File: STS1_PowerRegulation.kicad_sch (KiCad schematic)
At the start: 7 parts, among them U3 MCP1725-3302E_MC

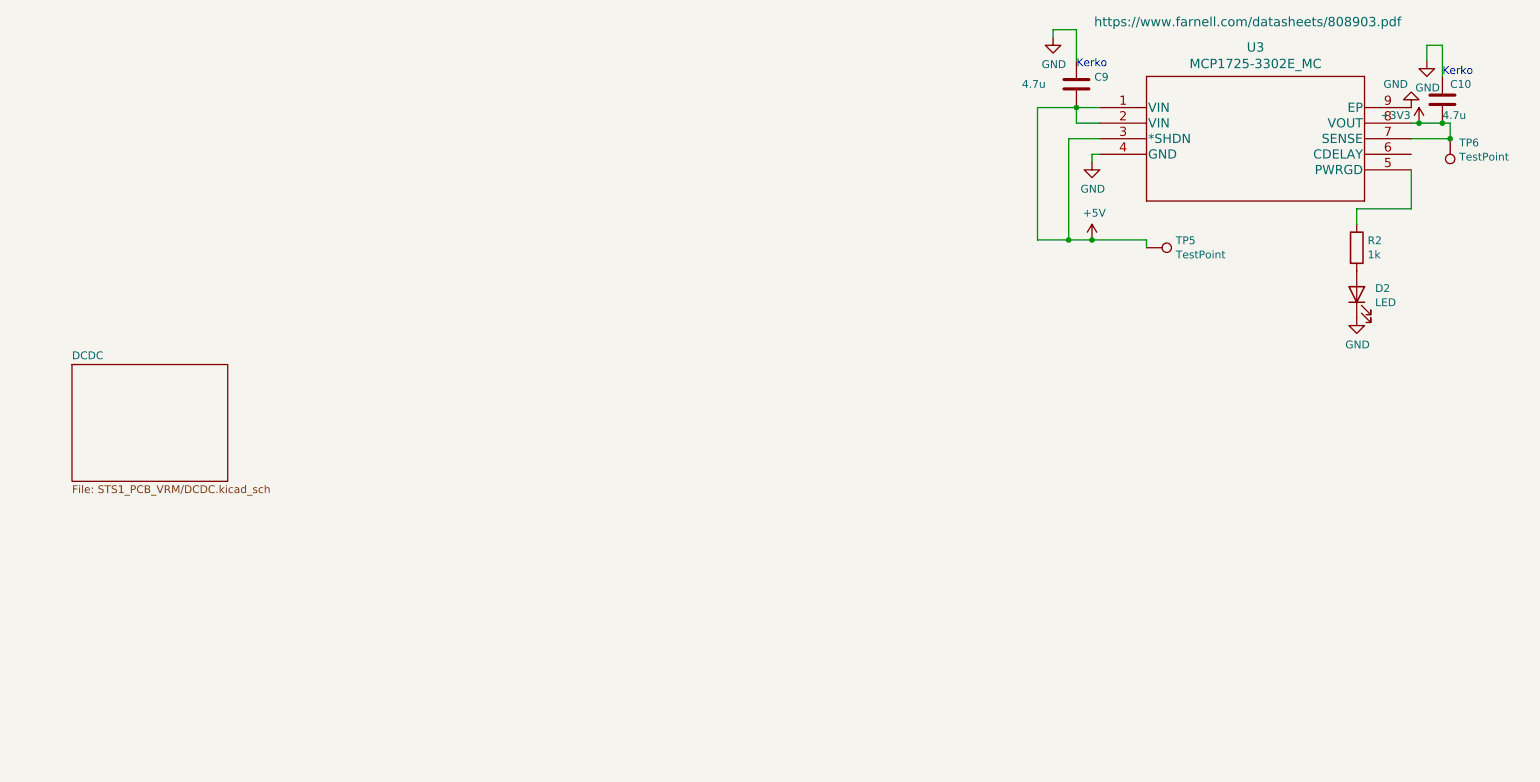
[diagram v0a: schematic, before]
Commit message: more work done
All parts besides RF added
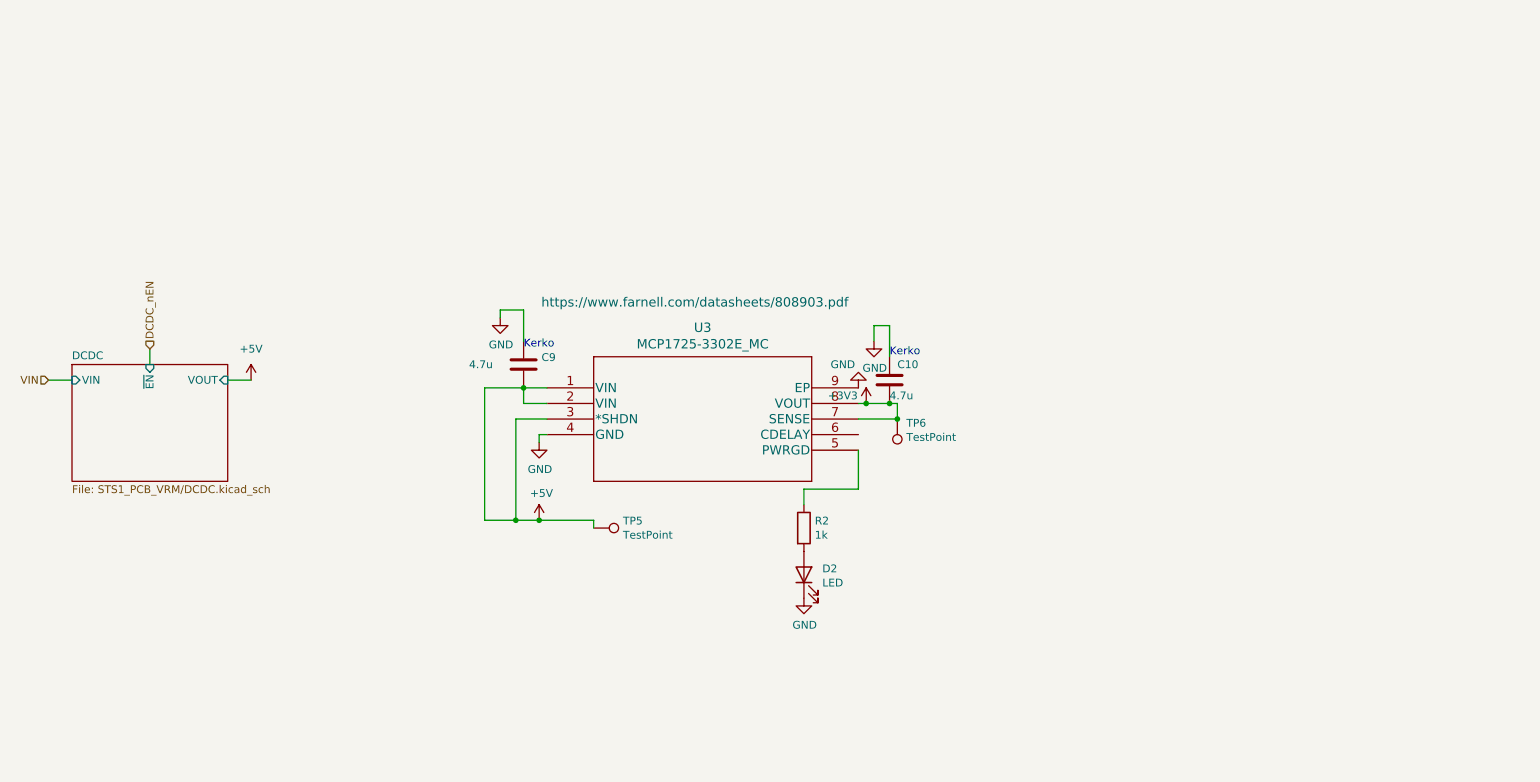
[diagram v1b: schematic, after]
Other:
- sheet DCDC ports: added VIN, VOUT, ~{EN}; removed none
- moved on the sheet: C10, C9, D2, R2, TP5, TP6, U3

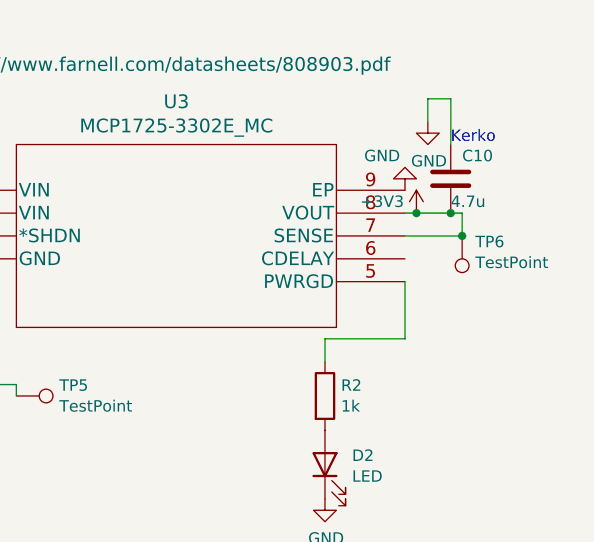
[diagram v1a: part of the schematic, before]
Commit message: add RF part
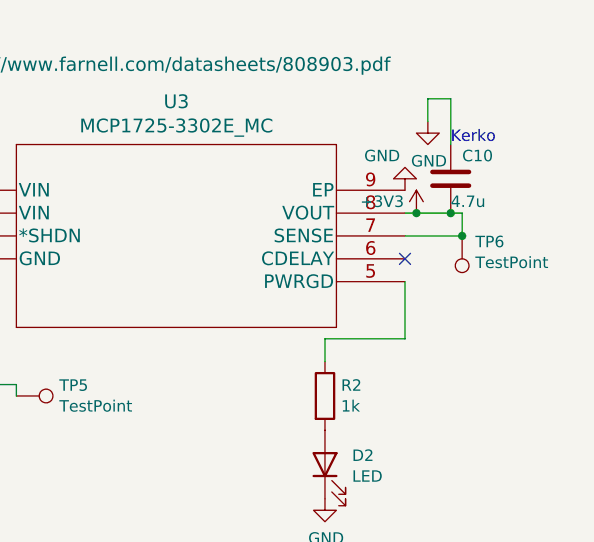
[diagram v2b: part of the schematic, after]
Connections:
- no-connect marks 0 -> 1
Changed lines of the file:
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@@
   (junction (at 130.81 102.87) (diameter 0) (color 0 0 0 0)
   )
+  (no_connect (at 186.69 88.9))
   (wire (pts (xy 83.82 80.01) (xy 87.63 80.01))
     (stroke (width 0) (type default) (color 0 0 0 0))

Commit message: V2.5
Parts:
- added D5, D6: LED, LED_SMD:LED_0805_2012Metric, symbol Device:LED
- added R32, R33: 220R, Resistor_SMD:R_0805_2012Metric, symbol Device:R
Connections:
- net +3V3: now also R33.1
- net +5V: now also R32.1
- net GND: now also D5.1 (K), D6.1 (K)
- new net: D6.2 (A), R33.2
- new net: D5.2 (A), R32.2
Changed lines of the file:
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@@
     (pin "1")
+  )
+  (symbol (lib_id "Device:R") (at 71.12 126.365 0) (unit 1)
+    (in_bom yes) (on_board yes)
+    (property "Reference" "R33" (id 0) (at 72.898 125.1966 0)
+      (effects (font (size 1.27 1.27)) (justify left))
+    )
+    (property "Value" "220R" (id 1) (at 72.898 127.508 0)
+      (effects (font (size 1.27 1.27)) (justify left))
+    )
+    (property "Footprint" "Resistor_SMD:R_0805_2012Metric" (id 2) (at 69.342 126.365 90)
+      (effects (font (size 1.27 1.27)) hide)
+    )
+    (property "Datasheet" "~" (id 3) (at 71.12 126.365 0)
+      (effects (font (size 1.27 1.27)) hide)
+    )
+    (pin "1")
+    (pin "2")
+  )
+  (symbol (lib_id "power:+3V3") (at 71.12 122.555 0) (unit 1)
+    (in_bom yes) (on_board yes) (fields_autoplaced)
+    (property "Reference" "#PWR037" (id 0) (at 71.12 126.365 0)
+      (effects (font (size 1.27 1.27)) hide)
+    )
+    (property "Value" "+3V3" (id 1) (at 71.12 116.84 0))
+    (property "Footprint" "" (id 2) (at 71.12 122.555 0)
+      (effects (font (size 1.27 1.27)) hide)
+    )
+    (property "Datasheet" "" (id 3) (at 71.12 122.555 0)
+      (effects (font (size 1.27 1.27)) hide)
+    )
+    (pin "1")
+  )
+  (symbol (lib_id "Device:LED") (at 57.15 133.985 90) (unit 1)
+    (in_bom yes) (on_board yes)
+    (property "Reference" "D5" (id 0) (at 60.1472 132.9944 90)
+      (effects (font (size 1.27 1.27)) (justify right))
+    )
+    (property "Value" "LED" (id 1) (at 60.1472 135.3058 90)
+      (effects (font (size 1.27 1.27)) (justify right))
+    )
+    (property "Footprint" "LED_SMD:LED_0805_2012Metric" (id 2) (at 57.15 133.985 0)
+      (effects (font (size 1.27 1.27)) hide)
+    )
+    (property "Datasheet" "~" (id 3) (at 57.15 133.985 0)
+      (effects (font (size 1.27 1.27)) hide)
+    )
+    (pin "1")
+    (pin "2")
   )
   (symbol (lib_id "power:+5V") (at 87.63 80.01 0) (unit 1)
@@
     (pin "1")
   )
+  (symbol (lib_id "power:GND") (at 71.12 137.795 0) (unit 1)
+    (in_bom yes) (on_board yes)
+    (property "Reference" "#PWR038" (id 0) (at 71.12 144.145 0)
+      (effects (font (size 1.27 1.27)) hide)
+    )
+    (property "Value" "GND" (id 1) (at 71.247 142.1892 0))
+    (property "Footprint" "" (id 2) (at 71.12 137.795 0)
+      (effects (font (size 1.27 1.27)) hide)
+    )
+    (property "Datasheet" "" (id 3) (at 71.12 137.795 0)
+      (effects (font (size 1.27 1.27)) hide)
+    )
+    (pin "1")
+  )
+  (symbol (lib_id "power:+5V") (at 57.15 122.555 0) (unit 1)
+    (in_bom yes) (on_board yes) (fields_autoplaced)
+    (property "Reference" "#PWR028" (id 0) (at 57.15 126.365 0)
+      (effects (font (size 1.27 1.27)) hide)
+    )
+    (property "Value" "+5V" (id 1) (at 57.15 116.84 0))
+    (property "Footprint" "" (id 2) (at 57.15 122.555 0)
+      (effects (font (size 1.27 1.27)) hide)
+    )
+    (property "Datasheet" "" (id 3) (at 57.15 122.555 0)
+      (effects (font (size 1.27 1.27)) hide)
+    )
+    (pin "1")
+  )
+  (symbol (lib_id "power:GND") (at 57.15 137.795 0) (unit 1)
+    (in_bom yes) (on_board yes)
+    (property "Reference" "#PWR029" (id 0) (at 57.15 144.145 0)
+      (effects (font (size 1.27 1.27)) hide)
+    )
+    (property "Value" "GND" (id 1) (at 57.277 142.1892 0))
+    (property "Footprint" "" (id 2) (at 57.15 137.795 0)
+      (effects (font (size 1.27 1.27)) hide)
+    )
+    (property "Datasheet" "" (id 3) (at 57.15 137.795 0)
+      (effects (font (size 1.27 1.27)) hide)
+    )
+    (pin "1")
+  )
+  (symbol (lib_id "Device:LED") (at 71.12 133.985 90) (unit 1)
+    (in_bom yes) (on_board yes)
+    (property "Reference" "D6" (id 0) (at 74.1172 132.9944 90)
+      (effects (font (size 1.27 1.27)) (justify right))
+    )
+    (property "Value" "LED" (id 1) (at 74.1172 135.3058 90)
+      (effects (font (size 1.27 1.27)) (justify right))
+    )
+    (property "Footprint" "LED_SMD:LED_0805_2012Metric" (id 2) (at 71.12 133.985 0)
+      (effects (font (size 1.27 1.27)) hide)
+    )
+    (property "Datasheet" "~" (id 3) (at 71.12 133.985 0)
+      (effects (font (size 1.27 1.27)) hide)
+    )
+    (pin "1")
+    (pin "2")
+  )
+  (symbol (lib_id "Device:R") (at 57.15 126.365 0) (unit 1)
+    (in_bom yes) (on_board yes)
+    (property "Reference" "R32" (id 0) (at 58.928 125.1966 0)
+      (effects (font (size 1.27 1.27)) (justify left))
+    )
+    (property "Value" "220R" (id 1) (at 58.928 127.508 0)
+      (effects (font (size 1.27 1.27)) (justify left))
+    )
+    (property "Footprint" "Resistor_SMD:R_0805_2012Metric" (id 2) (at 55.372 126.365 90)
+      (effects (font (size 1.27 1.27)) hide)
+    )
+    (property "Datasheet" "~" (id 3) (at 57.15 126.365 0)
+      (effects (font (size 1.27 1.27)) hide)
+    )
+    (pin "1")
+    (pin "2")
+  )
   (sheet (at 58.42 77.47) (size 25.4 19.05) (fields_autoplaced)

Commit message: Set all passive components (except in the RF path) to 0603
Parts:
- C10, C9: footprint Capacitor_SMD:C_0805_2012Metric -> Capacitor_SMD:C_0603_1608Metric
- R2, R32, R33: footprint Resistor_SMD:R_0805_2012Metric -> Resistor_SMD:R_0603_1608Metric
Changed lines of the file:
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@@
       (effects (font (size 1.27 1.27)) (justify left))
     )
-    (property "Footprint" "Resistor_SMD:R_0805_2012Metric" (id 2) (at 176.022 104.14 90)
+    (property "Footprint" "Resistor_SMD:R_0603_1608Metric" (id 2) (at 176.022 104.14 90)
       (effects (font (size 1.27 1.27)) hide)
     )
@@
       (effects (font (size 1.27 1.27)) (justify left))
     )
-    (property "Footprint" "Capacitor_SMD:C_0805_2012Metric" (id 2) (at 133.0452 81.28 0)
+    (property "Footprint" "Capacitor_SMD:C_0603_1608Metric" (id 2) (at 133.0452 81.28 0)
       (effects (font (size 1.27 1.27)) hide)
     )
@@
       (effects (font (size 1.27 1.27)) (justify left))
     )
-    (property "Footprint" "Capacitor_SMD:C_0805_2012Metric" (id 2) (at 192.7352 83.82 0)
+    (property "Footprint" "Capacitor_SMD:C_0603_1608Metric" (id 2) (at 192.7352 83.82 0)
       (effects (font (size 1.27 1.27)) hide)
     )
@@
       (effects (font (size 1.27 1.27)) (justify left))
     )
-    (property "Footprint" "Resistor_SMD:R_0805_2012Metric" (id 2) (at 69.342 126.365 90)
+    (property "Footprint" "Resistor_SMD:R_0603_1608Metric" (id 2) (at 69.342 126.365 90)
       (effects (font (size 1.27 1.27)) hide)
     )
@@
       (effects (font (size 1.27 1.27)) (justify left))
     )
-    (property "Footprint" "Resistor_SMD:R_0805_2012Metric" (id 2) (at 55.372 126.365 90)
-      (effects (font (size 1.27 1.27)) hide)
-    )
+    (property "Footprint" "Resistor_SMD:R_0603_1608Metric" (id 2) (at 55.372 126.365 90)
+      (effects (font (size 1.27 1.27)) hide)
+    )

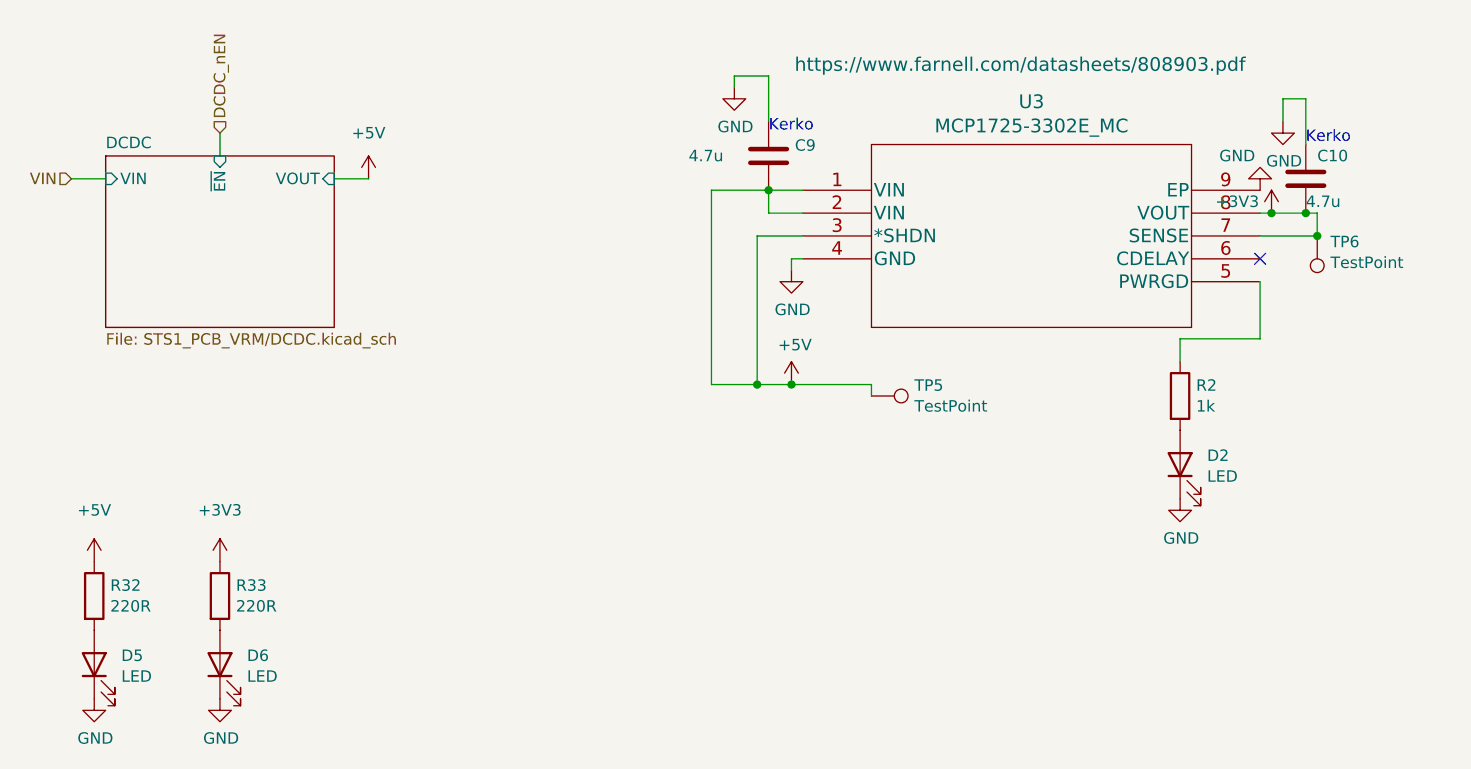
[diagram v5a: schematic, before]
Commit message: feat: update RF hardware and clean up ERC errors
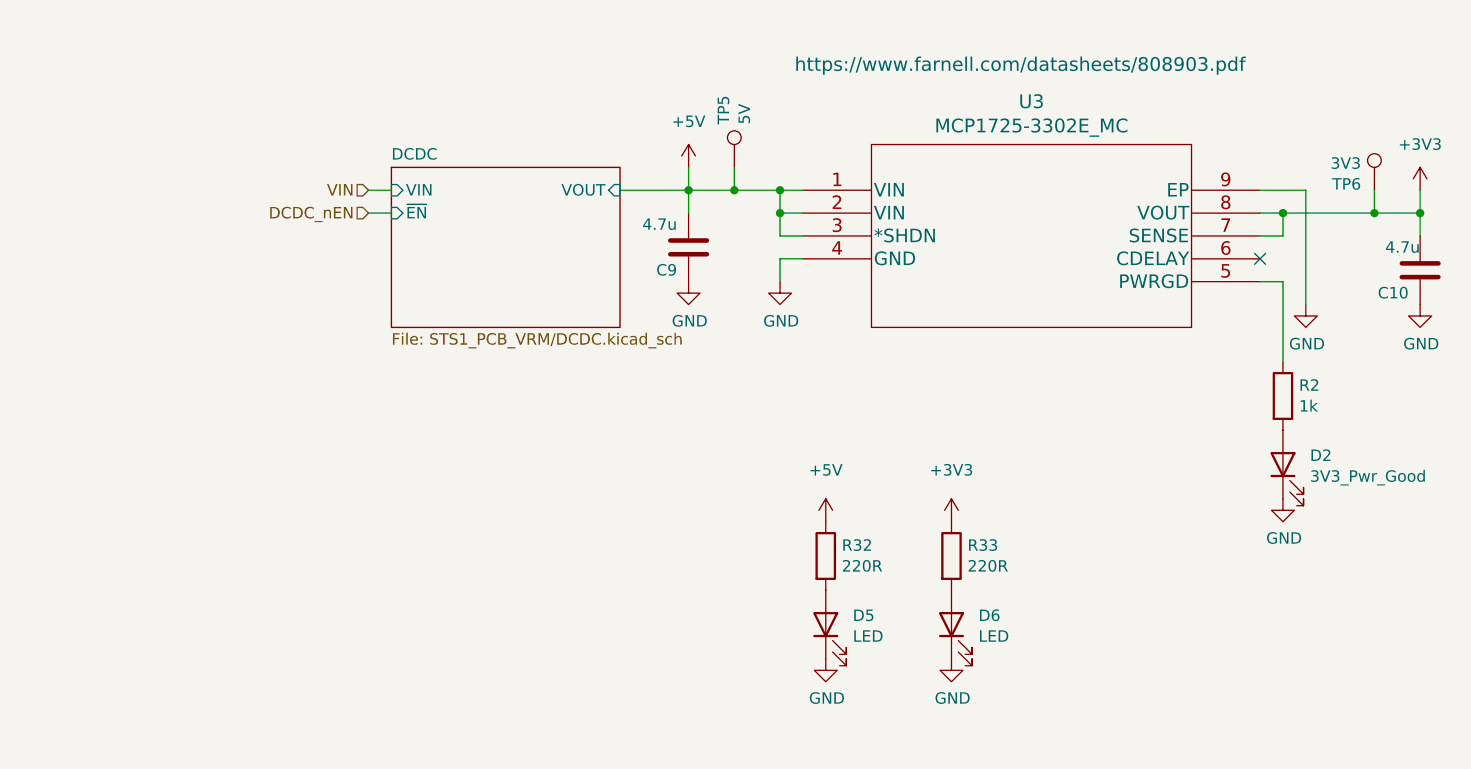
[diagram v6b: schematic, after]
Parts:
- D2: value LED -> 3V3_Pwr_Good
- TP5: value TestPoint -> 5V
- TP6: value TestPoint -> 3V3
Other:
- note removed: "Kerko"
- moved on the sheet: C10, C9, D2, D5, D6, R2, R32, R33, TP5, TP6

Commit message: feat: more schematic cleanup
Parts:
- C10, C9: value 4.7u -> 4.7µ
- R32, R33: value 220R -> 220
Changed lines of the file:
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@@
       (effects (font (size 1.27 1.27)) (justify left))
     )
-    (property "Value" "4.7u" (id 1) (at 121.92 85.09 0)
+    (property "Value" "4.7µ" (id 1) (at 121.92 85.09 0)
       (effects (font (size 1.27 1.27)) (justify left))
     )
@@
       (effects (font (size 1.27 1.27)) (justify left))
     )
-    (property "Value" "4.7u" (id 1) (at 204.47 87.63 0)
+    (property "Value" "4.7µ" (id 1) (at 204.47 87.63 0)
       (effects (font (size 1.27 1.27)) (justify left))
     )
@@
       (effects (font (size 1.27 1.27)) (justify left))
     )
-    (property "Value" "220R" (id 1) (at 154.178 123.063 0)
+    (property "Value" "220" (id 1) (at 154.178 123.063 0)
       (effects (font (size 1.27 1.27)) (justify left))
     )
@@
       (effects (font (size 1.27 1.27)) (justify left))
     )
-    (property "Value" "220R" (id 1) (at 140.208 123.063 0)
-      (effects (font (size 1.27 1.27)) (justify left))
-    )
+    (property "Value" "220" (id 1) (at 140.208 123.063 0)
+      (effects (font (size 1.27 1.27)) (justify left))
+    )

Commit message: Exclude jumpers, mounting holes, fiducials etc. from BOM
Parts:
- TP5: now left out of the parts list
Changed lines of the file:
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@@
   )
   (symbol (lib_id "Connector:TestPoint") (at 128.27 78.74 0) (unit 1)
-    (in_bom yes) (on_board yes)
+    (in_bom no) (on_board yes)
     (property "Reference" "TP5" (id 0) (at 127.1016 73.9648 90)
       (effects (font (size 1.27 1.27)) (justify left))
